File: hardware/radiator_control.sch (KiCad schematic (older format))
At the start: 42 parts, among them IC1 ATMEGA169PA-A, J1 Conn_01x29, J2 USB_B_Mini, M1 motor, Q1 Q_PMOS_SDG, Q2 Q_PMOS_SDG, Q3 BSS138, Q4 BSS138, SW1 Rotary_Encoder, SW2 SW_Push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

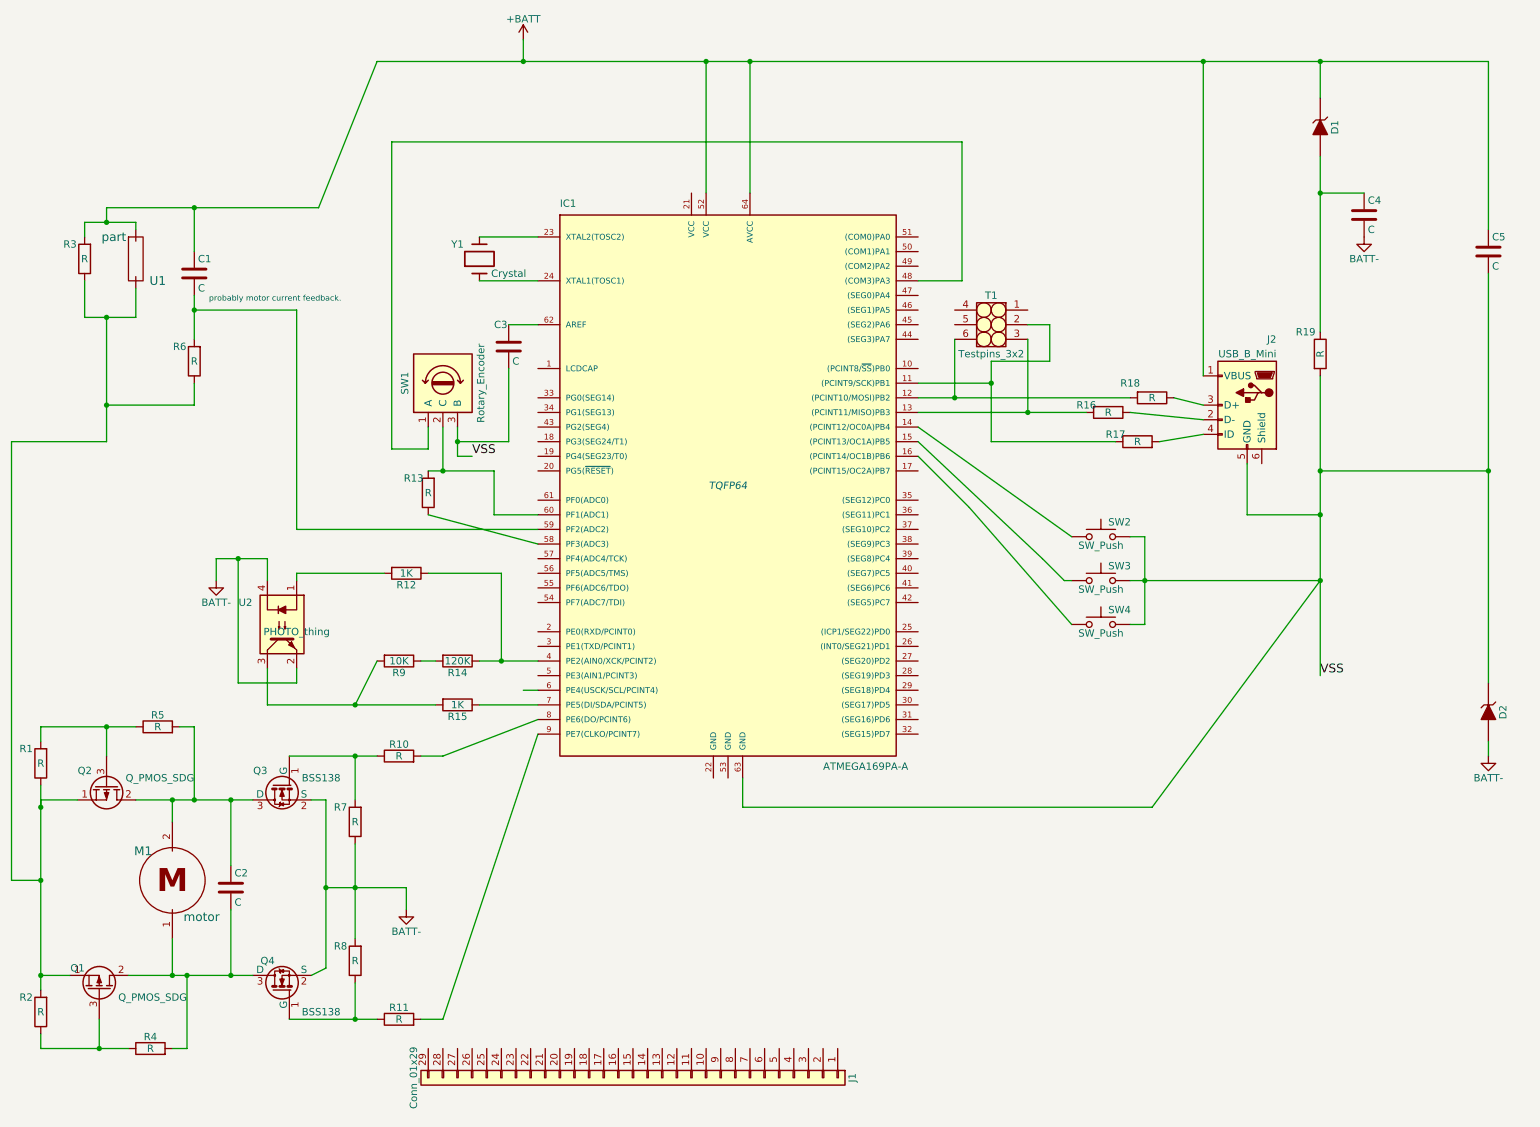
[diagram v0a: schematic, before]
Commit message: - add missing lcd connections - only one parts lib path
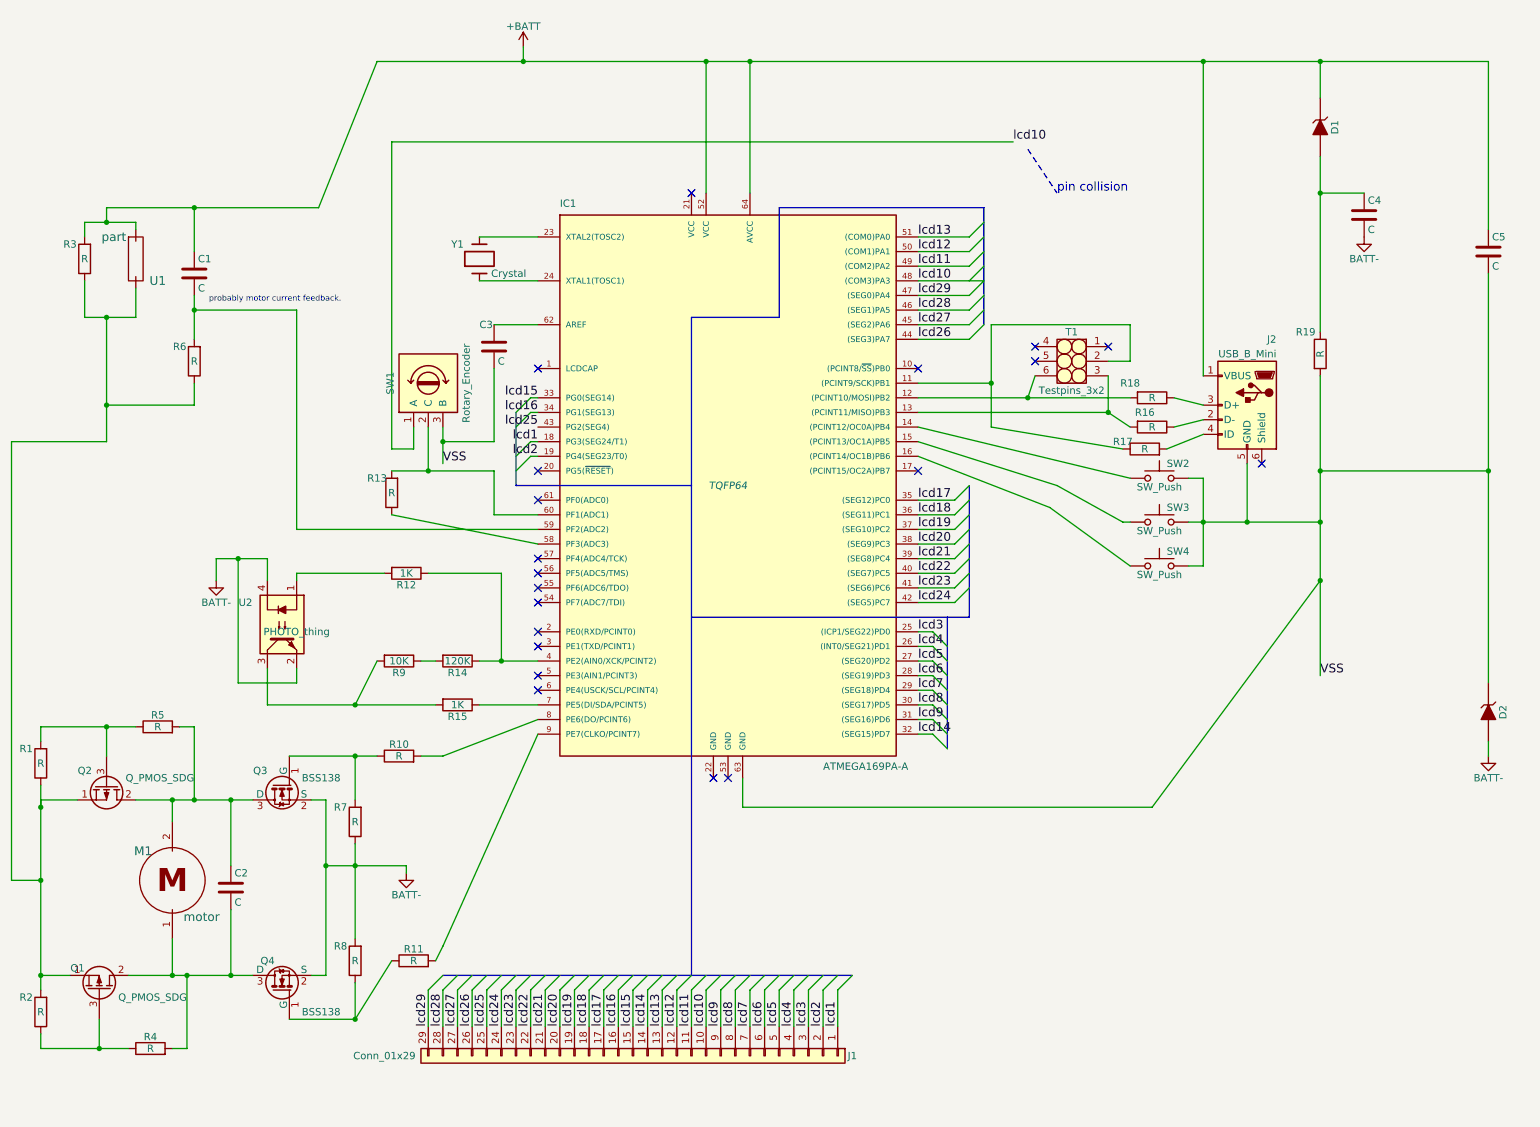
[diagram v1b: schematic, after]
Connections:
- net lcd1: now reaches IC1.18 (PG3(SEG24/T1))
- net lcd1: now also J1.1 (Pin_1)
- net lcd2: now reaches IC1.19 (PG4(SEG23/T0))
- net lcd2: now also J1.2 (Pin_2)
- net lcd3: now reaches IC1.25 ((ICP1/SEG22)PD0)
- net lcd3: now also J1.3 (Pin_3)
- net lcd4: now reaches IC1.26 ((INT0/SEG21)PD1)
- net lcd4: now also J1.4 (Pin_4)
- net lcd5: now reaches IC1.27 ((SEG20)PD2)
- net lcd5: now also J1.5 (Pin_5)
- net lcd6: now reaches IC1.28 ((SEG19)PD3)
- net lcd6: now also J1.6 (Pin_6)
- net lcd7: now reaches IC1.29 ((SEG18)PD4)
- net lcd7: now also J1.7 (Pin_7)
- net lcd8: now reaches IC1.30 ((SEG17)PD5)
- net lcd8: now also J1.8 (Pin_8)
- net lcd9: now reaches IC1.31 ((SEG16)PD6)
- net lcd9: now also J1.9 (Pin_9)
- net lcd14: now reaches IC1.32 ((SEG15)PD7)
- net lcd14: now also J1.14 (Pin_14)
- net lcd15: now reaches IC1.33 (PG0(SEG14))
- net lcd15: now also J1.15 (Pin_15)
- net lcd16: now reaches IC1.34 (PG1(SEG13))
- net lcd16: now also J1.16 (Pin_16)
- net lcd17: now reaches IC1.35 ((SEG12)PC0)
- net lcd17: now also J1.17 (Pin_17)
- net lcd18: now reaches IC1.36 ((SEG11)PC1)
- net lcd18: now also J1.18 (Pin_18)
- net lcd19: now reaches IC1.37 ((SEG10)PC2)
- net lcd19: now also J1.19 (Pin_19)
- net lcd20: now reaches IC1.38 ((SEG9)PC3)
- net lcd20: now also J1.20 (Pin_20)
- net lcd21: now reaches IC1.39 ((SEG8)PC4)
- net lcd21: now also J1.21 (Pin_21)
- net lcd22: now reaches IC1.40 ((SEG7)PC5)
- net lcd22: now also J1.22 (Pin_22)
- net lcd23: now reaches IC1.41 ((SEG6)PC6)
- net lcd23: now also J1.23 (Pin_23)
- net lcd24: now reaches IC1.42 ((SEG5)PC7)
- net lcd24: now also J1.24 (Pin_24)
- net lcd25: now reaches IC1.43 (PG2(SEG4))
- net lcd25: now also J1.25 (Pin_25)
- net lcd26: now reaches IC1.44 ((SEG3)PA7)
- net lcd26: now also J1.26 (Pin_26)
- net lcd27: now reaches IC1.45 ((SEG2)PA6)
- net lcd27: now also J1.27 (Pin_27)
- net lcd28: now reaches IC1.46 ((SEG1)PA5)
- net lcd28: now also J1.28 (Pin_28)
- net lcd29: now reaches IC1.47 ((SEG0)PA4)
- net lcd29: now also J1.29 (Pin_29)
- net lcd10: now reaches IC1.48 ((COM3)PA3), SW1.1 (A)
- net lcd10: now also J1.10 (Pin_10)
- net lcd11: now reaches IC1.49 ((COM2)PA2)
- net lcd11: now also J1.11 (Pin_11)
- net lcd12: now reaches IC1.50 ((COM1)PA1)
- net lcd12: now also J1.12 (Pin_12)
- net lcd13: now reaches IC1.51 ((COM0)PA0)
- net lcd13: now also J1.13 (Pin_13)
- no-connect marks 0 -> 20
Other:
- note added: "pin collision"
- moved on the sheet: C3, J1, R11, R13, R16, R17, SW1, SW2, SW3, SW4, T1

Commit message: * update
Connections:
- net lcd11 is gone; now on net lcd10: IC1.49 ((COM2)PA2), J1.11 (Pin_11)
- net lcd13 is gone; now on net blue: IC1.51 ((COM0)PA0), J1.13 (Pin_13)
- net lcd15 is gone; now on net lcd14: IC1.33 (PG0(SEG14)), J1.15 (Pin_15)
- net lcd17 is gone; now on net lcd16: IC1.35 ((SEG12)PC0), J1.17 (Pin_17)
- net lcd21 is gone; now on net green: IC1.39 ((SEG8)PC4), J1.21 (Pin_21)
- net lcd23 is gone; now on net lcd22: IC1.41 ((SEG6)PC6), J1.23 (Pin_23)
- net lcd25 is gone; now on net brown: IC1.43 (PG2(SEG4)), J1.25 (Pin_25)
- net lcd9 is gone; now on net black: IC1.31 ((SEG16)PD6), J1.9 (Pin_9)
- net at IC1.5 (PE3(AIN1/PCINT3)): now also R14.2, R9.1
- net lcd12 renamed blue
- net lcd19 renamed grey
- net lcd20 renamed green
- net lcd24 renamed brown
- net lcd8 renamed black
- no-connect marks 20 -> 19
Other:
- note added: "isp programming\n###########\nSCK : Blue on adapter cable\nMISO : Green\nMOSI : White\n\nReset: lila\n\n"
- note added: "my output wiring,\nsoldered to lcd pads"
- note added: "pa 1,0"
- note added: "pa 3,2"
- note added: "pc 3,4"
- note added: "pc 5,6 (did not work)"
- note added: "pc2"
- note added: "pc7, pg2"
- note added: "pd 5,6"
- note added: "pd7, pg0\n"
- note added: "pg1, pc0"
- note added: "somehow like this\n"
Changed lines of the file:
@@
 EESchema Schematic File Version 2
 LIBS:parts
+LIBS:power
 LIBS:radiator_control-cache
 EELAYER 25 0
@@
 U 1 1 5B49E957
 P 4850 7650
-F 0 "J1" V 4850 9150 50  0000 C CNN
-F 1 "Conn_01x29" V 4850 5950 50  0000 C CNN
+F 0 "J1" H 4850 9150 50  0000 C CNN
+F 1 "Conn_01x29" H 4850 6150 50  0000 C CNN
 F 2 "" H 4850 7650 50  0001 C CNN
 F 3 "" H 4850 7650 50  0001 C CNN
@@
 	-1   0    0    1
 $EndComp
-Text Label 9550 5050 0    60   ~ 0
+Text Label 10050 3900 0    60   ~ 0
 VSS
 Text Label 3550 3600 0    60   ~ 0
@@
 NoConn ~ 4200 3850
 NoConn ~ 4200 3650
-NoConn ~ 4200 5050
 NoConn ~ 4200 5150
 NoConn ~ 4200 4850
@@
 	1    0    0    -1
 $EndComp
+$Comp
+L BATT- #PWR05
+U 1 1 5B4B8349
+P 9850 2050
+F 0 "#PWR05" H 9850 1800 50  0001 C CNN
+F 1 "BATT-" H 9850 1900 50  0000 C CNN
+F 2 "" H 9850 2050 50  0001 C CNN
+F 3 "" H 9850 2050 50  0001 C CNN
+	1    9850 2050
+	1    0    0    -1
+$EndComp
+Text Label 9050 6350 2    60   ~ 0
+lcd8
+Text Label 9050 6250 2    60   ~ 0
+lcd9
+Text Label 9050 6150 2    60   ~ 0
+lcd10
+Text Label 9050 6050 2    60   ~ 0
+lcd11
+Text Label 9050 5950 2    60   ~ 0
+lcd12
+Text Label 9050 5850 2    60   ~ 0
+lcd13
+Text Label 9050 5750 2    60   ~ 0
+lcd14
+Text Label 9050 5650 2    60   ~ 0
+lcd15
+Text Label 9050 5550 2    60   ~ 0
+lcd16
+Text Label 9050 5450 2    60   ~ 0
+lcd17
+Text Label 9050 5250 2    60   ~ 0
+lcd19
+Text Label 9050 5150 2    60   ~ 0
+lcd20
+Text Label 9050 5050 2    60   ~ 0
+lcd21
+Text Label 9050 4950 2    60   ~ 0
+lcd22
+Text Label 9050 4850 2    60   ~ 0
+lcd23
+Text Label 9050 4750 2    60   ~ 0
+lcd24
+Text Label 9050 4650 2    60   ~ 0
+lcd25
+Text Label 9400 6300 0    60   ~ 0
+black
+Text Label 9400 6100 0    60   ~ 0
+white
+Text Label 9400 5900 0    60   ~ 0
+blue
+Text Label 9400 5700 0    60   ~ 0
+yellow
+Text Label 9400 5500 0    60   ~ 0
+red
+Text Label 9400 5300 0    60   ~ 0
+grey
+Text Label 9400 5100 0    60   ~ 0
+green
+Text Label 9400 4900 0    60   ~ 0
+purple
+Text Label 9400 4700 0    60   ~ 0
+brown
+Text Notes 7800 6350 0    59   ~ 0
+my output wiring,\nsoldered to lcd pads
+Text Notes 9750 6300 0    60   ~ 0
+pd 5,6
+Text Notes 9750 6100 0    60   ~ 0
+pa 3,2
+Text Notes 9750 5900 0    60   ~ 0
+pa 1,0
+Text Notes 9750 5700 0    60   ~ 0
+pd7, pg0\n
+Text Notes 9750 5500 0    60   ~ 0
+pg1, pc0
+Text Notes 9750 5300 0    60   ~ 0
+pc2
+Text Notes 9750 5100 0    60   ~ 0
+pc 3,4
+Text Notes 9750 4900 0    60   ~ 0
+pc 5,6 (did not work)
+Text Notes 9750 4700 0    60   ~ 0
+pc7, pg2
+Text Notes 7800 2600 0    60   ~ 0
+ isp programming\n###########\nSCK : Blue on adapter cable\nMISO : Green\nMOSI : White\n\nReset: lila\n\n
 Wire Wire Line
 	3550 5600 4200 5350
@@
 	9550 4000 8650 4000
 Wire Wire Line
-	9550 3000 9550 5050
+	9550 3000 9550 4450
 Wire Wire Line
 	9550 3650 10700 3650
@@
 Connection ~ 9550 850
 Connection ~ 9550 3650
-Connection ~ 9550 4400
 Wire Wire Line
 	8750 850  8750 3000
@@
 	3950 4350 3950 4950
 Wire Wire Line
-	3800 4950 4200 4950
-Connection ~ 3950 4950
-Wire Wire Line
 	3400 4950 3500 4950
 Wire Wire Line
@@
 	5600 5750 5600 5950
 Wire Wire Line
-	5600 5950 8400 5950
+	5600 5950 7250 5950
 Wire Wire Line
 	3900 2650 4200 2650
@@
 	3550 7100 6350 7100
 Wire Wire Line
-	8400 5950 9550 4400
+	7250 5950 7250 4650
 Connection ~ 9550 4000
 Wire Bus Line
@@
 Wire Wire Line
 	4150 3450 4200 3450
-$Comp
-L BATT- #PWR05
-U 1 1 5B4B8349
-P 9850 2050
-F 0 "#PWR05" H 9850 1800 50  0001 C CNN
-F 1 "BATT-" H 9850 1900 50  0000 C CNN
-F 2 "" H 9850 2050 50  0001 C CNN
-F 3 "" H 9850 2050 50  0001 C CNN
-	1    9850 2050
-	1    0    0    -1
-$EndComp
+Wire Wire Line
+	9250 6350 9050 6350
+Wire Wire Line
+	9050 6250 9250 6250
+Wire Wire Line
+	9250 6150 9050 6150
+Wire Wire Line
+	9050 6050 9250 6050
+Wire Wire Line
+	9250 5950 9050 5950
+Wire Wire Line
+	9050 5850 9250 5850
+Wire Wire Line
+	9250 5750 9050 5750
+Wire Wire Line
+	9050 5650 9250 5650
+Wire Wire Line
+	9250 5550 9050 5550
+Wire Wire Line
+	9050 5450 9250 5450
+Wire Wire Line
+	9050 5250 9250 5250
+Wire Wire Line
+	9250 5150 9050 5150
+Wire Wire Line
+	9050 5050 9250 5050
+Wire Wire Line
+	9250 6250 9250 6350
+Wire Wire Line
+	9250 6050 9250 6150
+Wire Wire Line
+	9250 5850 9250 5950
+Wire Wire Line
+	9250 5650 9250 5750
+Wire Wire Line
+	9250 5450 9250 5550
+Wire Wire Line
+	9250 5050 9250 5150
+Wire Wire Line
+	9250 5100 9400 5100
+Connection ~ 9250 5100
+Wire Wire Line
+	9250 5300 9400 5300
+Wire Wire Line
+	9250 5500 9400 5500
+Connection ~ 9250 5500
+Wire Wire Line
+	9250 5700 9400 5700
+Connection ~ 9250 5700
+Wire Wire Line
+	9250 5900 9400 5900
+Connection ~ 9250 5900
+Wire Wire Line
+	9250 6100 9400 6100
+Connection ~ 9250 6100
+Wire Wire Line
+	9250 6300 9400 6300
+Connection ~ 9250 6300
+Wire Wire Line
+	10050 3650 10050 3900
+Connection ~ 10050 3650
+Wire Notes Line
+	10250 6450 10250 4500
+Wire Wire Line
+	9250 5250 9250 5300
+Wire Wire Line
+	9250 4950 9050 4950
+Wire Wire Line
+	9050 4850 9250 4850
+Wire Wire Line
+	9250 4850 9250 4950
+Wire Wire Line
+	9250 4900 9400 4900
+Connection ~ 9250 4900
+Wire Wire Line
+	9250 4750 9050 4750
+Wire Wire Line
+	9050 4650 9250 4650
+Wire Wire Line
+	9250 4650 9250 4750
+Wire Wire Line
+	9250 4700 9400 4700
+Connection ~ 9250 4700
+Wire Notes Line
+	10250 4500 8750 4500
+Wire Notes Line
+	8750 4500 8750 6450
+Wire Notes Line
+	8750 6450 10250 6450
+Wire Wire Line
+	7250 4650 8500 4650
+Wire Wire Line
+	8500 4650 8500 4450
+Wire Wire Line
+	8500 4450 9550 4450
+Wire Notes Line
+	6650 3050 7750 2300
+Wire Wire Line
+	3450 4950 3450 5150
+Wire Wire Line
+	3450 5150 4050 5150
+Wire Wire Line
+	4050 5150 4050 5050
+Wire Wire Line
+	4050 5050 4200 5050
+Connection ~ 3450 4950
+Wire Wire Line
+	3800 4950 4200 4950
+Connection ~ 3950 4950
+Wire Notes Line
+	2850 4600 2850 5400
+Wire Notes Line
+	2850 5400 3900 5400
+Wire Notes Line
+	3900 5400 3900 5300
+Wire Notes Line
+	3900 5300 4100 5300
+Wire Notes Line
+	4100 5300 4100 4600
+Wire Notes Line
+	4100 4600 2850 4600
+Text Notes 2950 4750 0    60   ~ 0
+somehow like this\n
 $EndSCHEMATC
